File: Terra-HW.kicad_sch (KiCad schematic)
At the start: 0 parts

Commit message: Added MCU and started power section.
Signed-off-by: James Mendel <jrm.mendel@gmail.com>
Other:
- added sheet Microcontroller (Microcontroller.kicad_sch)
- added sheet Power (Power.kicad_sch)
- title: Microcontroller -> ${TITLE}
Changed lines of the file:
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@@
 	(paper "A4")
 	(title_block
-		(title "Microcontroller")
+		(title "${TITLE}")
 		(date "2025-03-15")
 		(rev "${REVISION}")
 		(company "J. MENDEL")
-		(comment 1 "${TITLE}")
+	)
+	(text_box "Sheet: ${SHEETNAME}"
+		(exclude_from_sim no)
+		(at 177.8 167.64 0)
+		(size 106.68 12.7)
+		(margins 0.9525 0.9525 0.9525 0.9525)
+		(stroke
+			(width -0.0001)
+			(type solid)
+		)
+		(fill
+			(type none)
+		)
+		(effects
+			(font
+				(face "KiCad Font")
+				(size 3 3)
+				(thickness 0.254)
+				(bold yes)
+				(color 0 0 0 1)
+			)
+			(justify left)
+		)
+	)
+	(sheet
+		(at 114.3 73.66)
+		(size 27.94 17.78)
+		(exclude_from_sim no)
+		(in_bom yes)
+		(on_board yes)
+		(dnp no)
+		(fields_autoplaced yes)
+		(stroke
+			(width 0.1524)
+			(type solid)
+		)
+		(fill
+			(color 0 0 0 0.0000)
+		)
+		(property "Sheetname" "Power"
+			(at 114.3 72.9484 0)
+			(effects
+				(font
+					(size 1.27 1.27)
+				)
+				(justify left bottom)
+			)
+		)
+		(property "Sheetfile" "Power.kicad_sch"
+			(at 114.3 92.0246 0)
+			(effects
+				(font
+					(size 1.27 1.27)
+				)
+				(justify left top)
+			)
+		)
+		(instances
+			(project "Terra-HW"
+				(path "/acca4a2f-1cc7-44b0-a26a-921257f6c268"
+					(page "3")
+				)
+			)
+		)
+	)
+	(sheet
+		(at 114.3 99.06)
+		(size 27.94 17.78)
+		(exclude_from_sim no)
+		(in_bom yes)
+		(on_board yes)
+		(dnp no)
+		(fields_autoplaced yes)
+		(stroke
+			(width 0.1524)
+			(type solid)
+		)
+		(fill
+			(color 0 0 0 0.0000)
+		)
+		(property "Sheetname" "Microcontroller"
+			(at 114.3 98.3484 0)
+			(effects
+				(font
+					(size 1.27 1.27)
+				)
+				(justify left bottom)
+			)
+		)
+		(property "Sheetfile" "Microcontroller.kicad_sch"
+			(at 114.3 117.4246 0)
+			(effects
+				(font
+					(size 1.27 1.27)
+				)
+				(justify left top)
+			)
+		)
+		(instances
+			(project "Terra-HW"
+				(path "/acca4a2f-1cc7-44b0-a26a-921257f6c268"
+					(page "2")
+				)
+			)
+		)
 	)
 	(sheet_instances

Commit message: Added power latch circuit.
Signed-off-by: James Mendel <jrm.mendel@gmail.com>
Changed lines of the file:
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@@
 	)
 	(sheet
-		(at 114.3 73.66)
+		(at 77.47 137.16)
 		(size 27.94 17.78)
 		(exclude_from_sim no)
@@
 		)
 		(property "Sheetname" "Power"
-			(at 114.3 72.9484 0)
+			(at 77.47 136.4484 0)
 			(effects
 				(font
@@
 		)
 		(property "Sheetfile" "Power.kicad_sch"
-			(at 114.3 92.0246 0)
+			(at 77.47 155.5246 0)
 			(effects
 				(font
@@
 	)
 	(sheet
-		(at 114.3 99.06)
+		(at 129.54 78.74)
 		(size 27.94 17.78)
 		(exclude_from_sim no)
@@
 		)
 		(property "Sheetname" "Microcontroller"
-			(at 114.3 98.3484 0)
+			(at 129.54 78.0284 0)
 			(effects
 				(font
@@
 		)
 		(property "Sheetfile" "Microcontroller.kicad_sch"
-			(at 114.3 117.4246 0)
+			(at 129.54 97.1046 0)
 			(effects
 				(font

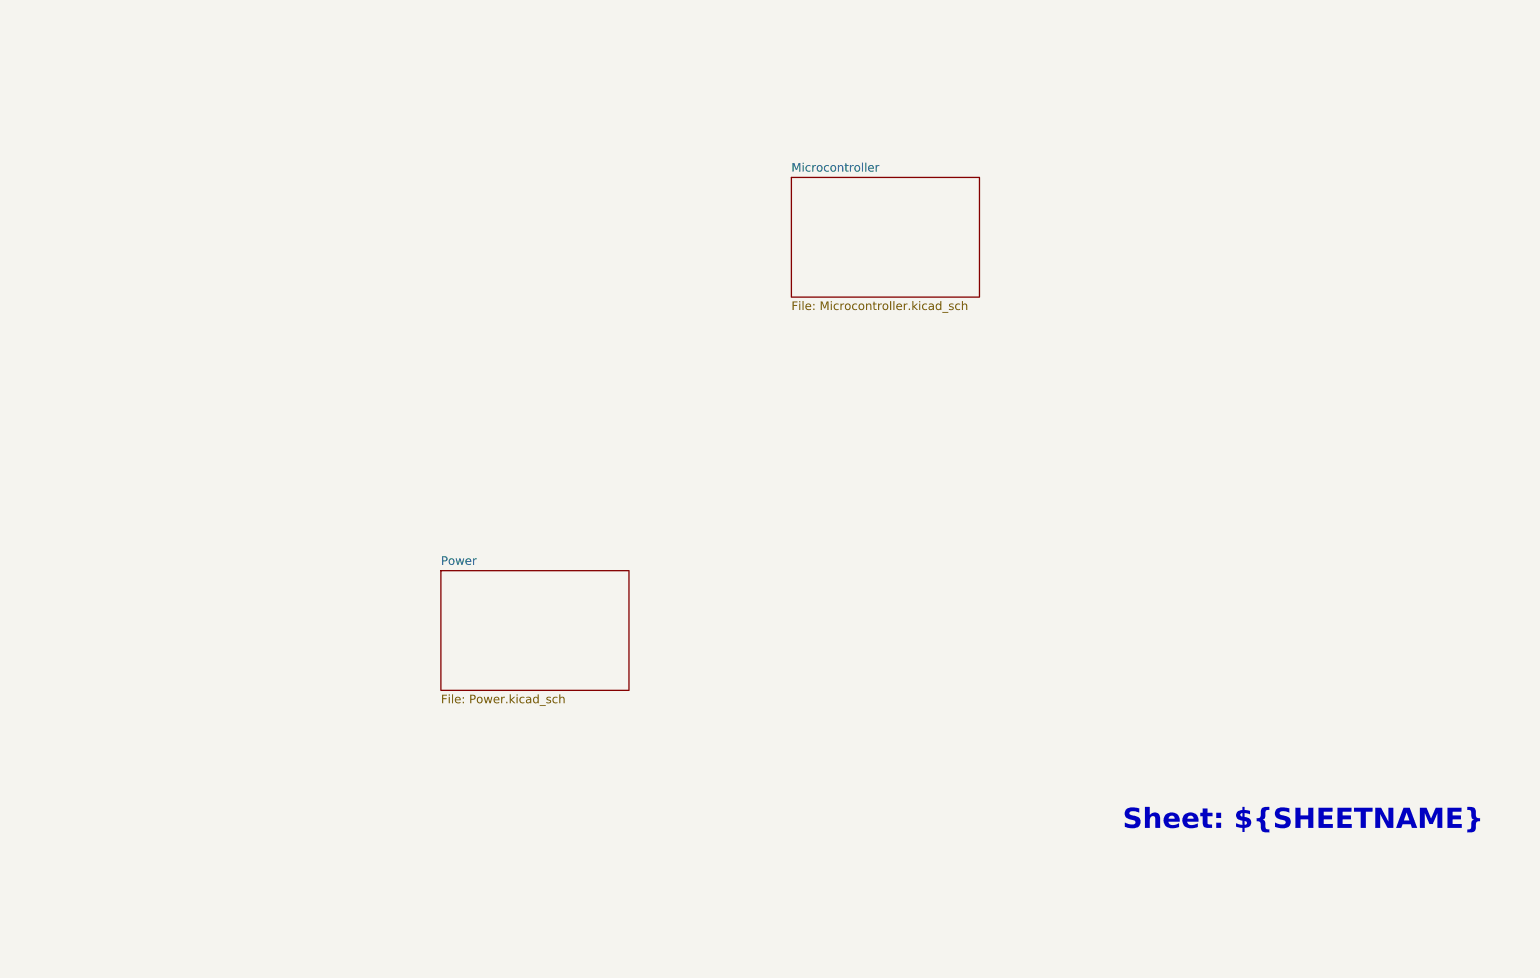
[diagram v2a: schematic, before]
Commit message: SCH and PCB updates. Added Integrated GPS and other features.
Signed-off-by: James Mendel <jrm.mendel@gmail.com>
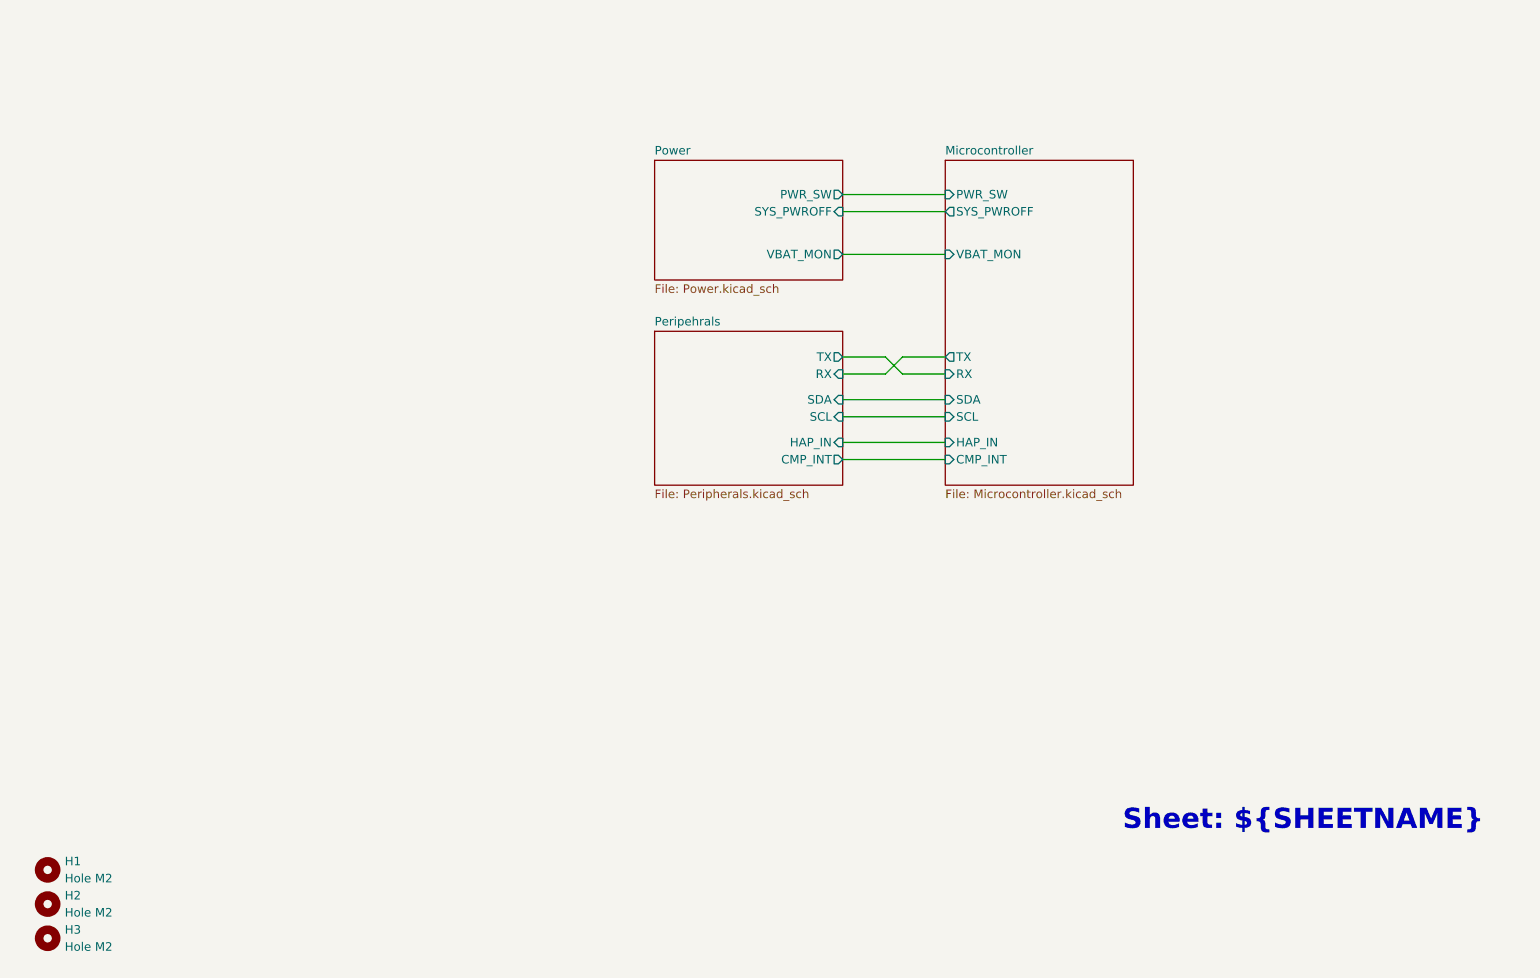
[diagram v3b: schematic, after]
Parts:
- added H1, H2, H3: Hole M2, MountingHole:MountingHole_2.2mm_M2, symbol Mechanical:MountingHole
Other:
- added sheet Peripehrals (Peripherals.kicad_sch)
- sheet Microcontroller ports: added CMP_INT, HAP_IN, PWR_SW, RX, SCL, SDA, SYS_PWROFF, TX, VBAT_MON; removed none
- sheet Power ports: added PWR_SW, SYS_PWROFF, VBAT_MON; removed none

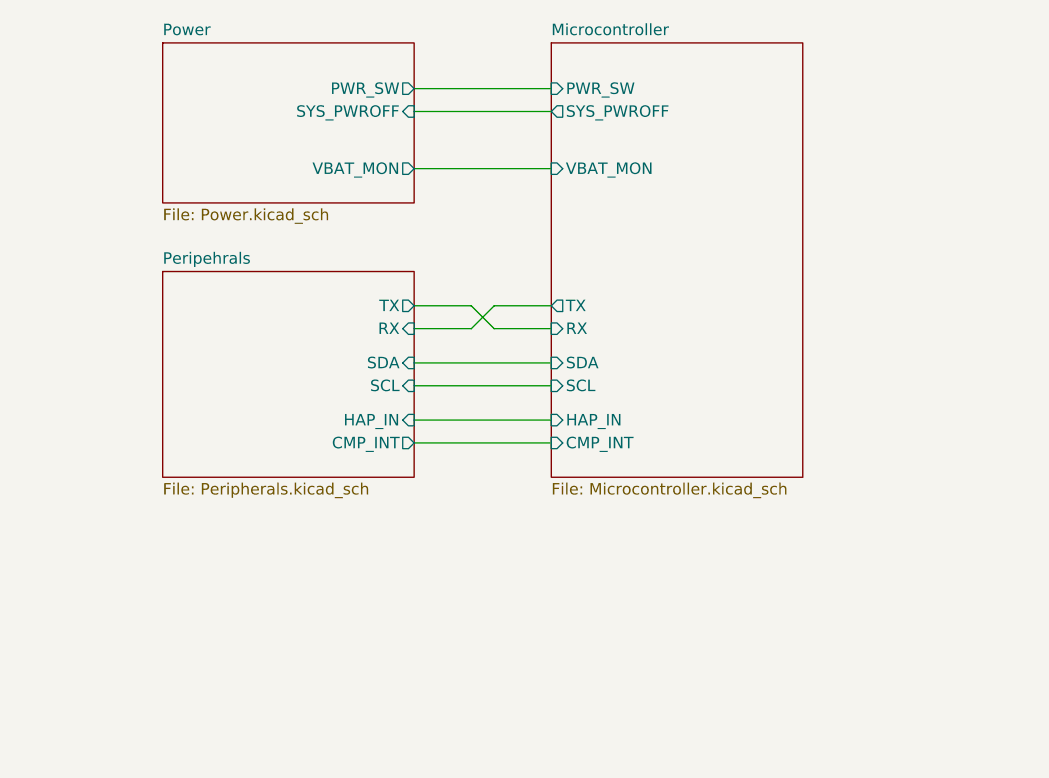
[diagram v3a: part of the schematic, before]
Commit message: Updated board outline to version 004
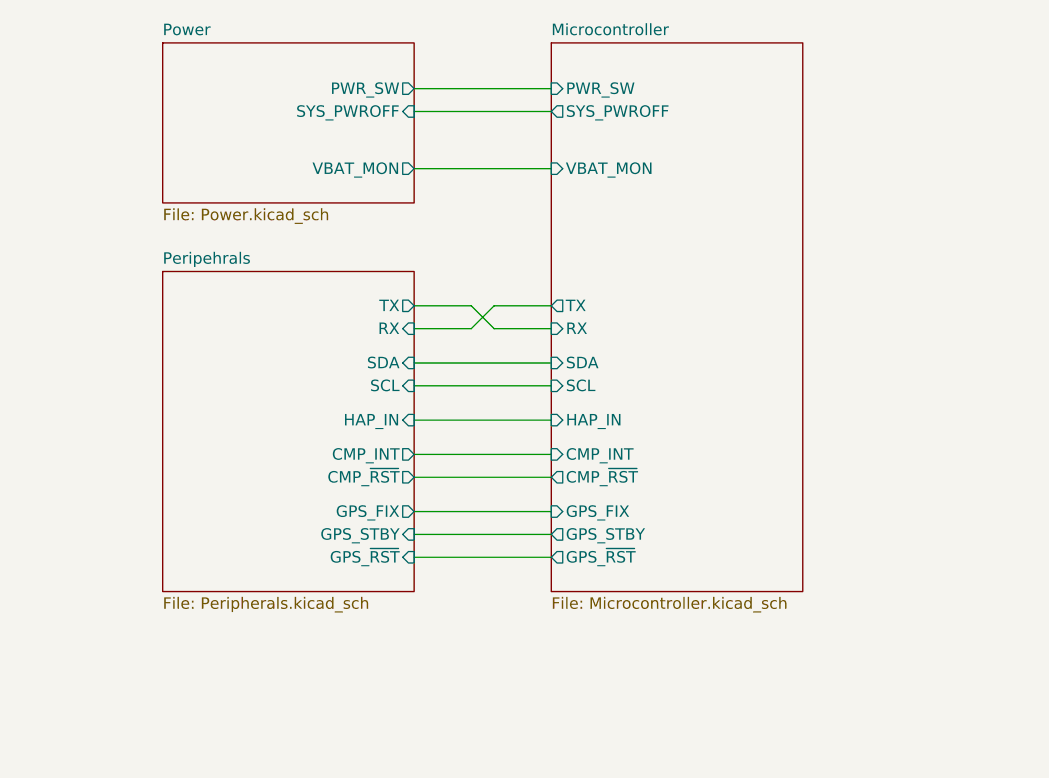
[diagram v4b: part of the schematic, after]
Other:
- sheet Microcontroller ports: added CMP_~{RST}, GPS_FIX, GPS_STBY, GPS_~{RST}; removed none
- sheet Peripehrals ports: added CMP_~{RST}, GPS_FIX, GPS_STBY, GPS_~{RST}; removed none
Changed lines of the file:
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@@
 	(wire
 		(pts
-			(xy 137.16 120.65) (xy 152.4 120.65)
+			(xy 137.16 130.81) (xy 152.4 130.81)
+		)
+		(stroke
+			(width 0)
+			(type default)
+		)
+	)
+	(wire
+		(pts
+			(xy 137.16 121.92) (xy 152.4 121.92)
 		)
 		(stroke
@@
 	(wire
 		(pts
+			(xy 137.16 128.27) (xy 152.4 128.27)
+		)
+		(stroke
+			(width 0)
+			(type default)
+		)
+	)
+	(wire
+		(pts
 			(xy 137.16 90.17) (xy 152.4 90.17)
 		)
@@
 	(wire
 		(pts
+			(xy 137.16 124.46) (xy 152.4 124.46)
+		)
+		(stroke
+			(width 0)
+			(type default)
+		)
+	)
+	(wire
+		(pts
 			(xy 137.16 83.82) (xy 152.4 83.82)
+		)
+		(stroke
+			(width 0)
+			(type default)
+		)
+	)
+	(wire
+		(pts
+			(xy 137.16 133.35) (xy 152.4 133.35)
 		)
 		(stroke
@@
 			"AAAAAAAAAAAAAAAAAAAAAAAAAAAAAAAAAAAAAAAAAAAAAAAAAAAAAAAAAAAAAAAAAAAAAAAAAAAA"
 			"AAAAAAAAAAAAAAAAAAAAAAAAAAAAAAAAAAAAAAAAAAAAAAAAAAAAAAAAAAAAAAAAAAAAAAAAAAAA"
+			"AAAAAAAAAAAAAAAAAAAAAAAAAAAAAAAAAAAAAAAAAAAAAAAAAAAAAAAAAAAAAAAAAAAAAAAAAAAA"
+			"AAAAAAAAAAAAAAAAAAAAAAAAAAAAAAAAAAAAAAAAAAAAAAAAAAAAAAAAAAAAAAAAAAAAAAAAAAAA"
+			"AAAAAAAAAAAAAAAAAAAAAAAAAAAAAAAAAAAAAAAAAAAAAAAAAAAAAAAAAAAAAAAAAAAAAAAAAAAA"
+			"AAAAAAAAAAAAAAAAAAAAAAAAAAAAAAAAAAAAAAAAAAAAAAAAAAAAAAAAAAAAAAAAAAAAAAAAAAAA"
+			"AAAAAAAAAAAAAAAAAAAAAAAAAAAAAAAAAAAAAAAAAAAAAAAAAAAAAAAAAAAAAAAAAAAAAAAAAAAA"
+			"AAAAAAAAAAAAAAAAAAAAAAAAAAAAAAAAAAAAAAAAAAAAAAAAAAAAAAAAAAAAAAAAAAAAAAAAAAAA"
+			"AAAAAAAAAAAAAAAAAAAAAAAAAAAAAAAAAAAAAAAAAAAAAAAAAAAAAAAAAAAAAAAAAAAAAAAAAAAA"
+			"AAAAAAAAAAAAAAAAAAAAAAAAAAAAAAAAAAAAAAAAAAAAAAAAAAAAAAAAAAAAAAAAAAAAAAAAAAAA"
+			"AAAAAAAAAAAAAAAAAAAAAAAAAAAAAAAAAAAAAAAAAAAAAAAAAAAAAAAAAAAAAAAAAAAAAAAAAAAA"
+			"AAAAAAAAAAAAAAAAAAAAAAAAAAAAAAAAAAAAAAAAAAAAAAAAAAAAAAAAAAAAAAAAAAAAAAAAAAAA"
+			"AAAAAAAAAAAAAAAAAAAAAAAAAAAAAAAAAAAAAAAAAAAAAAAAAAAAAAAAAAAAAAAAAAAAAAAAAAAA"
+			"AAAAAAAAAAAAAAAAAAAAAAAAAAAAAAAAAAAAAAAAAAAAAAAAAAAAAAAAAAAAAAAAAAAAAAAAAAAA"
+			"AAAAAAAAAAAAAAAAAAAAAAAAAAAAAAAAAAAAAAAAAAAAAAAAAAAAAAAAAAAAAAAAAAAAAAAAAAAA"
+			"AAAAAAAAAAAAAAAAAAAAAAAAAAAAAAAAAAAAAAAAAAAAAAAAAAAAAAAAAAAAAAAAAAAAAAAAAAAA"
+			"AAAAAAAAAAAAAAAAAAAAAAAAAAAAAAAAAAAAAAAAAAAAAAAAAAAAAAAAAAAAAAAAAAAAAAAAAAAA"
+			"AAAAAAAAAAAAAAAAAAAAAAAAAAAAAAAAAAAAAAAAAAAAAAAAAAAAAAAAAAAAAAAAAAAAAAAAAAAA"
+			"AAAAAAAAAAAAAAAAAAAAAAAAAAAAAAAAAAAAAAAAAAAAAAAAAAAAAAAAAAAAAAAAAAAAAAAAAAAA"
+			"AAAAAAAAAAAAAAAAAAAAAAAAAAAAAAAAAAAAAAAAAAAAAAAAAAAAAAAAAAAAAAAAAAAAAAAAAAAA"
 			"AAAAAAAAAAAAAAAAAAAAAAAAAAAAAAAAAAAAAAAAAAAAAAAAAA=="
 		)
@@
 		(at 19.05 181.61 0)
 		(unit 1)
-		(exclude_from_sim yes)
+		(exclude_from_sim no)
 		(in_bom no)
 		(on_board yes)
@@
 		(at 19.05 186.69 0)
 		(unit 1)
-		(exclude_from_sim yes)
+		(exclude_from_sim no)
 		(in_bom no)
 		(on_board yes)
@@
 		(at 19.05 191.77 0)
 		(unit 1)
-		(exclude_from_sim yes)
+		(exclude_from_sim no)
 		(in_bom no)
 		(on_board yes)
@@
 	(sheet
 		(at 109.22 101.6)
-		(size 27.94 22.86)
+		(size 27.94 35.56)
 		(exclude_from_sim no)
 		(in_bom yes)
@@
 		)
 		(property "Sheetfile" "Peripherals.kicad_sch"
-			(at 109.22 125.0446 0)
+			(at 109.22 137.7446 0)
 			(effects
 				(font
@@
 		)
 		(pin "CMP_INT" output
-			(at 137.16 120.65 0)
+			(at 137.16 121.92 0)
+			(effects
+				(font
+					(size 1.27 1.27)
+				)
+				(justify right)
+			)
+		)
+		(pin "GPS_FIX" output
+			(at 137.16 128.27 0)
+			(effects
+				(font
+					(size 1.27 1.27)
+				)
+				(justify right)
+			)
+		)
+		(pin "GPS_STBY" input
+			(at 137.16 130.81 0)
+			(effects
+				(font
+					(size 1.27 1.27)
+				)
+				(justify right)
+			)
+		)
+		(pin "CMP_~{RST}" output
+			(at 137.16 124.46 0)
+			(effects
+				(font
+					(size 1.27 1.27)
+				)
+				(justify right)
+			)
+		)
+		(pin "GPS_~{RST}" input
+			(at 137.16 133.35 0)
 			(effects
 				(font
@@
 	(sheet
 		(at 152.4 76.2)
-		(size 27.94 48.26)
+		(size 27.94 60.96)
 		(exclude_from_sim no)
 		(in_bom yes)
@@
 		)
 		(property "Sheetfile" "Microcontroller.kicad_sch"
-			(at 152.4 125.0446 0)
+			(at 152.4 137.7446 0)
 			(effects
 				(font
@@
 		)
 		(pin "CMP_INT" input
-			(at 152.4 120.65 180)
-			(effects
-				(font
+			(at 152.4 121.92 180)
+			(effects
+				(font
+					(size 1.27 1.27)
+				)
+				(justify left)
+			)
+		)
+		(pin "GPS_STBY" output
+			(at 152.4 130.81 180)
+			(effects
+				(font
+					(size 1.27 1.27)
+				)
+				(justify left)
+			)
+		)
+		(pin "GPS_~{RST}" output
+			(at 152.4 133.35 180)
+			(effects
+				(font
+					(size 1.27 1.27)
+				)
+				(justify left)
+			)
+		)
+		(pin "GPS_FIX" input
+			(at 152.4 128.27 180)
+			(effects
+				(font
+					(size 1.27 1.27)
+				)
+				(justify left)
+			)
+		)
+		(pin "CMP_~{RST}" output
+			(at 152.4 124.46 180)
+			(effects
+				(font
